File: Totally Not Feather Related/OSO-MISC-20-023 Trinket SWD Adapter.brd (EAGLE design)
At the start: 15.2 x 19.9 mm, 7 parts, among them X2 2x5 0.05" SWD

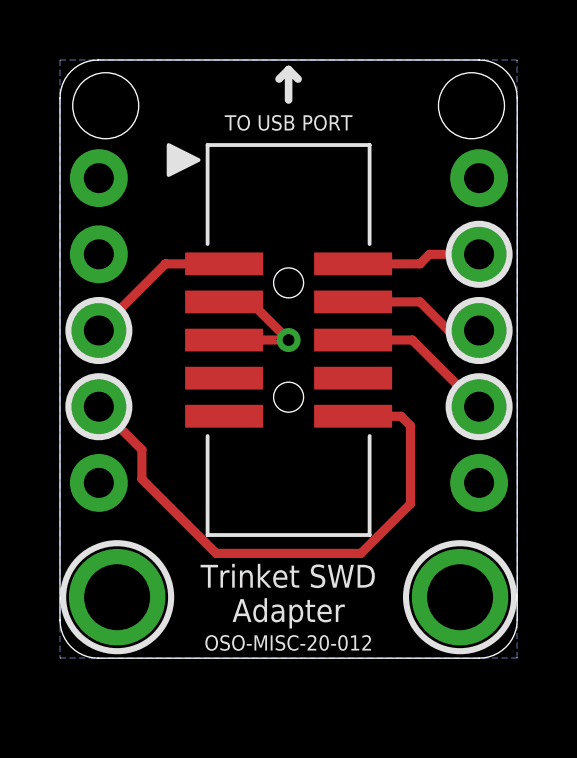
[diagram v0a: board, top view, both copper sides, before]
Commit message: update trinket SWD adapter
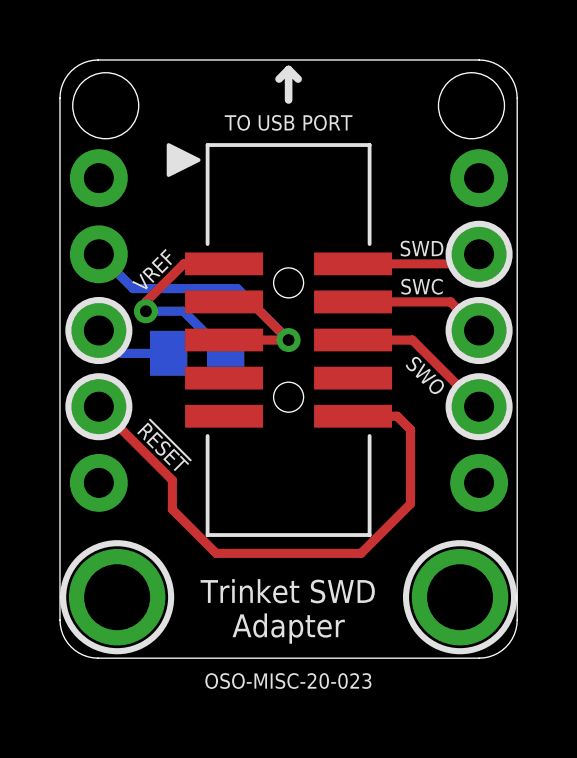
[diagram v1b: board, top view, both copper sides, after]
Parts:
- added R1: 100K, microbuilder:0805-NO
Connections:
- new net MCU_3V3: R1.2, X2.1
- net VREF: now also R1.1; no longer X2.1
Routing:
- net GND: track 4.83 -> 12.3 mm
- net MCU_3V3: track 0.00 -> 6.69 mm, vias 0 -> 1
- net VREF: track 5.10 -> 2.64 mm
- removed copper zone on layer 16, net GND
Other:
- board text added: "!RESET"
- board text added: "OSO-MISC-20-023"
- board text added: "SWC"
- board text added: "SWD"
- board text added: "SWO"
- board text added: "VREF"
- board text removed: "OSO-MISC-20-012"
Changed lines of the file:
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@@
 <setting verticaltext="up"/>
 </settings>
-<grid distance="0.01" unitdist="inch" unit="inch" style="lines" multiple="1" display="no" altdistance="0.005" altunitdist="inch" altunit="inch"/>
+<grid distance="0.01" unitdist="inch" unit="inch" style="lines" multiple="1" display="no" altdistance="0.001" altunitdist="inch" altunit="inch"/>
 <layers>
 <layer number="1" name="Top" color="4" fill="1" visible="yes" active="yes"/>
@@
 <layer number="56" name="wert" color="7" fill="1" visible="no" active="yes"/>
 <layer number="57" name="tCAD" color="7" fill="1" visible="no" active="no"/>
+<layer number="58" name="b3D" color="7" fill="1" visible="no" active="no"/>
 <layer number="59" name="tCarbon" color="7" fill="1" visible="no" active="no"/>
 <layer number="60" name="bCarbon" color="7" fill="1" visible="no" active="no"/>
+<layer number="61" name="stand" color="7" fill="1" visible="no" active="no"/>
 <layer number="88" name="SimResults" color="9" fill="1" visible="no" active="no"/>
 <layer number="89" name="SimProbes" color="9" fill="1" visible="no" active="no"/>
@@
 <dimension x1="-5.7785" y1="12.7" x2="-6.096" y2="6.223" x3="-8.763" y3="9.4615" textsize="1.778" layer="47" dtype="vertical" unit="inch"/>
 <dimension x1="-6.0325" y1="-14.0335" x2="-5.715" y2="-10.16" x3="-8.509" y3="-12.09675" textsize="1.778" layer="47" dtype="vertical" unit="inch"/>
-<text x="0" y="-11.811" size="0.762" layer="21" font="vector" ratio="18" align="center">Trinket SWD
+<text x="0" y="-12.319" size="0.762" layer="21" font="vector" ratio="18" align="center">Trinket SWD
 Adapter</text>
-<text x="0" y="-13.462" size="0.508" layer="21" font="vector" ratio="13" align="center">OSO-MISC-20-012</text>
+<text x="0" y="-14.732" size="0.508" layer="21" font="vector" ratio="13" align="center">OSO-MISC-20-023</text>
 <text x="2.7305" y="-7.0485" size="0.762" layer="22" font="vector" ratio="18" rot="MR0" align="top-left">Pins:</text>
 <text x="2.7305" y="-7.0485" size="0.762" layer="22" font="vector" rot="MR0" align="top-left">
@@
 <text x="4.064" y="-3.81" size="0.508" layer="22" font="vector" ratio="13" rot="SMR270" align="center-left">Trinket SWD
 Adapter</text>
-<text x="-3.048" y="-2.032" size="0.508" layer="22" font="vector" rot="SMR270" align="center-left">For use with
+<text x="1.905" y="-1.016" size="0.508" layer="22" font="vector" rot="SMR270" align="center-left">For use with
 Trinket M0
 or PyRuler.</text>
+<text x="4.445" y="-0.3175" size="0.508" layer="21" font="vector" ratio="13" align="center">SWD</text>
+<text x="4.445" y="-1.5875" size="0.508" layer="21" font="vector" ratio="13" align="center">SWC</text>
+<text x="4.572" y="-4.5593" size="0.508" layer="21" font="vector" ratio="13" rot="R135" align="center">SWO</text>
+<text x="-4.4704" y="-1.0541" size="0.508" layer="21" font="vector" ratio="13" rot="R45" align="center">VREF</text>
+<text x="-4.2037" y="-6.9596" size="0.508" layer="21" font="vector" ratio="13" rot="R135" align="center">!RESET</text>
 </plain>
 <attributes>
@@
 <element name="U$1" library="My Stuff" package="OSO_BEAR_250X360MIL_1000DPI" value="" x="-0.762" y="1.778" smashed="yes" rot="MR270"/>
 <element name="U$2" library="My Stuff" package="OSO_WORDMARK_ONELINE_350MIL_1000DPI" value="" x="4.318" y="1.27" smashed="yes" rot="MR270"/>
+<element name="R1" library="microbuilder" package="0805-NO" value="100K" x="-3.048" y="-3.81" smashed="yes" rot="MR180">
+<attribute name="NAME" x="-3.175" y="-5.08" size="0.508" layer="26" font="vector" ratio="18" rot="MR180" align="center"/>
+<attribute name="VALUE" x="-1.016" y="-3.048" size="0.4064" layer="28" ratio="10" rot="MR180"/>
+</element>
 </elements>
 <signals>
 <signal name="GND">
-<polygon width="0.254" layer="16">
-<vertex x="-7.62" y="5.969"/>
-<vertex x="-7.62" y="-13.97"/>
-<vertex x="7.62" y="-13.97"/>
-<vertex x="7.62" y="5.969"/>
-</polygon>
 <contactref element="JP3" pad="2"/>
 <contactref element="X2" pad="3"/>
@@
 <wire x1="-2.15" y1="-2.0955" x2="-1.27" y2="-2.0955" width="0.3048" layer="1"/>
 <wire x1="-1.27" y1="-2.0955" x2="0" y2="-3.3655" width="0.3048" layer="1"/>
+<wire x1="-6.3246" y1="-0.508" x2="-5.1816" y2="-1.651" width="0.3048" layer="16"/>
+<wire x1="-1.7145" y1="-1.651" x2="-5.1816" y2="-1.651" width="0.3048" layer="16"/>
+<wire x1="-1.7145" y1="-1.651" x2="0" y2="-3.3655" width="0.3048" layer="16"/>
 </signal>
 <signal name="VBUS">
@@
 <contactref element="X2" pad="4"/>
 <contactref element="JP4" pad="3"/>
-<wire x1="2.15" y1="-2.0955" x2="4.3815" y2="-2.0955" width="0.3048" layer="1"/>
-<wire x1="5.334" y1="-3.048" x2="4.3815" y2="-2.0955" width="0.3048" layer="1"/>
-<wire x1="5.334" y1="-3.048" x2="6.35" y2="-3.048" width="0.3048" layer="1"/>
+<wire x1="2.15" y1="-2.0955" x2="5.3975" y2="-2.0955" width="0.3048" layer="1"/>
+<wire x1="6.35" y1="-3.048" x2="5.3975" y2="-2.0955" width="0.3048" layer="1"/>
 </signal>
 <signal name="SWDIO">
 <contactref element="X2" pad="2"/>
 <contactref element="JP4" pad="4"/>
-<wire x1="2.15" y1="-0.8255" x2="4.3815" y2="-0.8255" width="0.3048" layer="1"/>
-<wire x1="4.699" y1="-0.508" x2="4.3815" y2="-0.8255" width="0.3048" layer="1"/>
-<wire x1="4.699" y1="-0.508" x2="6.35" y2="-0.508" width="0.3048" layer="1"/>
+<wire x1="6.0325" y1="-0.8255" x2="2.15" y2="-0.8255" width="0.3048" layer="1"/>
+<wire x1="6.0325" y1="-0.8255" x2="6.35" y2="-0.508" width="0.3048" layer="1"/>
 </signal>
 <signal name="SWO">
@@
 <wire x1="4.1275" y1="-3.3655" x2="6.35" y2="-5.588" width="0.3048" layer="1"/>
 </signal>
-<signal name="VREF" class="1">
+<signal name="MCU_3V3" class="1">
 <contactref element="X2" pad="1"/>
-<contactref element="JP3" pad="3"/>
-<wire x1="-6.3246" y1="-3.048" x2="-4.1021" y2="-0.8255" width="0.3048" layer="1"/>
-<wire x1="-4.1021" y1="-0.8255" x2="-2.15" y2="-0.8255" width="0.3048" layer="1"/>
+<contactref element="R1" pad="2"/>
+<wire x1="-2.098" y1="-3.81" x2="-3.50135" y2="-2.40665" width="0.3048" layer="16"/>
+<wire x1="-3.50135" y1="-2.40665" x2="-4.75615" y2="-2.40665" width="0.3048" layer="16"/>
+<via x="-4.75615" y="-2.40665" extent="1-16" drill="0.3937"/>
+<wire x1="-4.75615" y1="-2.40665" x2="-4.75615" y2="-2.08915" width="0.3048" layer="1"/>
+<wire x1="-3.4925" y1="-0.8255" x2="-2.15" y2="-0.8255" width="0.3048" layer="1"/>
+<wire x1="-4.75615" y1="-2.08915" x2="-3.4925" y2="-0.8255" width="0.3048" layer="1"/>
 </signal>
 <signal name="!RESET">
 <contactref element="X2" pad="10"/>
 <contactref element="JP3" pad="4"/>
-<wire x1="2.15" y1="-5.9055" x2="3.7465" y2="-5.9055" width="0.3048" layer="1"/>
-<wire x1="3.7465" y1="-5.9055" x2="4.064" y2="-6.223" width="0.3048" layer="1"/>
-<wire x1="4.064" y1="-6.223" x2="4.064" y2="-8.8265" width="0.3048" layer="1"/>
+<wire x1="2.15" y1="-5.9055" x2="3.6195" y2="-5.9055" width="0.3048" layer="1"/>
+<wire x1="3.6195" y1="-5.9055" x2="4.064" y2="-6.35" width="0.3048" layer="1"/>
+<wire x1="4.064" y1="-6.35" x2="4.064" y2="-8.8265" width="0.3048" layer="1"/>
 <wire x1="4.064" y1="-8.8265" x2="2.413" y2="-10.4775" width="0.3048" layer="1"/>
 <wire x1="2.413" y1="-10.4775" x2="-2.413" y2="-10.4775" width="0.3048" layer="1"/>
-<wire x1="-2.413" y1="-10.4775" x2="-4.8895" y2="-8.001" width="0.3048" layer="1"/>
-<wire x1="-4.8895" y1="-8.001" x2="-4.8895" y2="-7.0231" width="0.3048" layer="1"/>
-<wire x1="-4.8895" y1="-7.0231" x2="-6.3246" y2="-5.588" width="0.3048" layer="1"/>
+<wire x1="-2.413" y1="-10.4775" x2="-3.8735" y2="-9.017" width="0.3048" layer="1"/>
+<wire x1="-3.8735" y1="-9.017" x2="-3.8735" y2="-8.0391" width="0.3048" layer="1"/>
+<wire x1="-3.8735" y1="-8.0391" x2="-6.3246" y2="-5.588" width="0.3048" layer="1"/>
+</signal>
+<signal name="VREF" class="1">
+<contactref element="JP3" pad="3"/>
+<contactref element="R1" pad="1"/>
+<wire x1="-3.998" y1="-3.81" x2="-5.5626" y2="-3.81" width="0.3048" layer="16"/>
+<wire x1="-5.5626" y1="-3.81" x2="-6.3246" y2="-3.048" width="0.3048" layer="16"/>
 </signal>
 </signals>
